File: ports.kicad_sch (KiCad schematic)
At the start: 0 parts

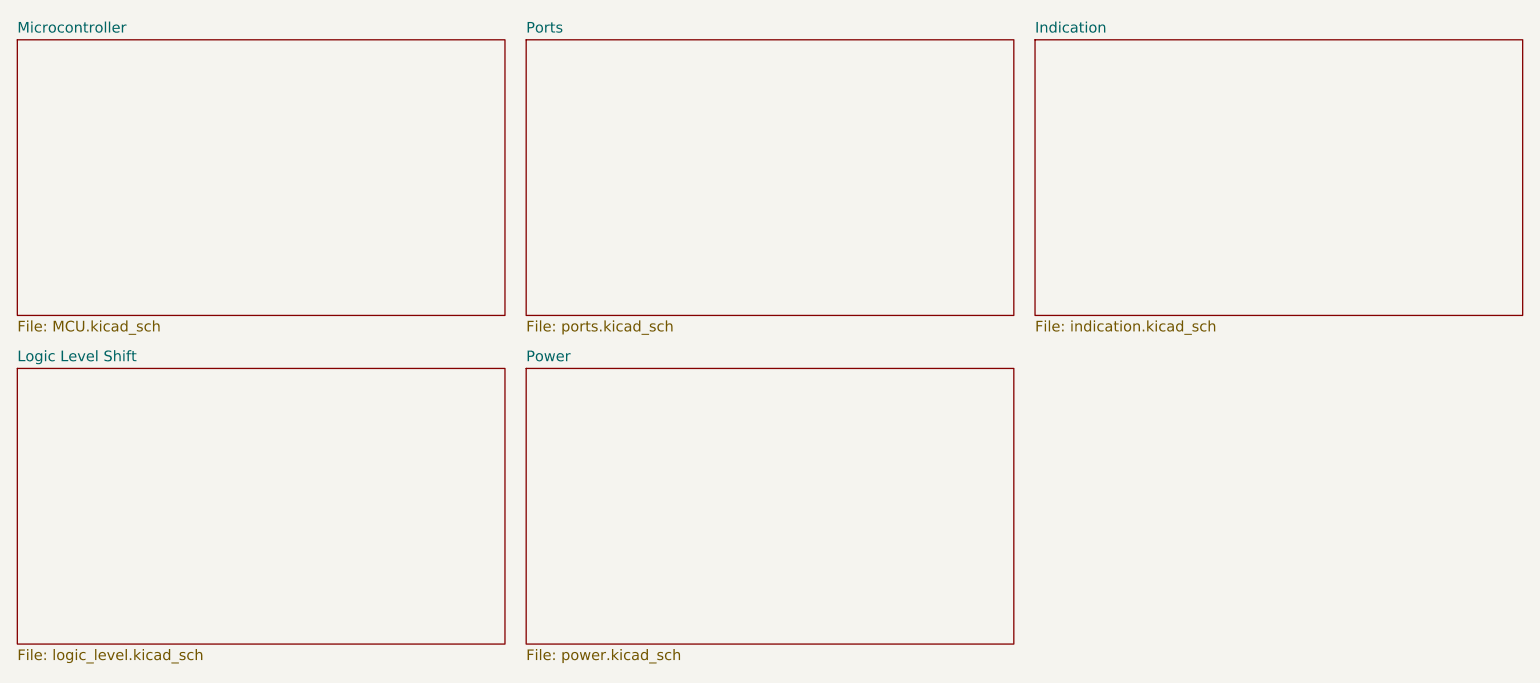
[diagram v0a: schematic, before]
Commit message: Break up schematic into hierarchical sheets
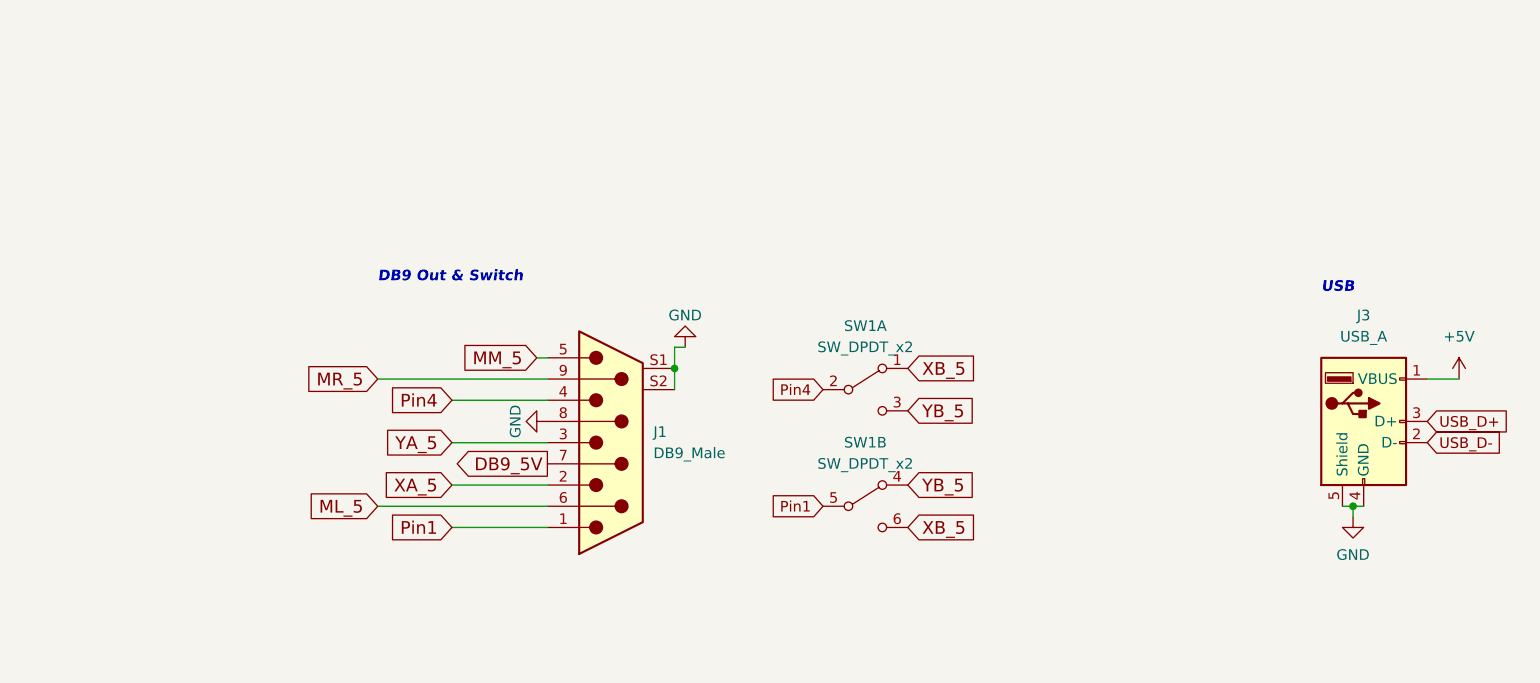
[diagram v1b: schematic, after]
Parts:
- added J1: DB9_Male, My Library:ASSMANN_A-DF_09_A_KG-T2S, symbol Connector:DB9_Male
- added J3: USB_A, Library:USB_A_China, symbol Connector:USB_A
- added SW1: SW_DPDT_x2, Button_Switch_SMD:SW_DPDT_CK_JS202011JCQN, symbol Switch:SW_DPDT_x2
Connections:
- new net +5V: J3.1 (VBUS)
- new net DB9_5V: J1.7
- new net GND: J1.8, J1.S1, J1.S2, J3.4 (GND), J3.5 (Shield)
- new net ML_5: J1.6
- new net MM_5: J1.5
- new net MR_5: J1.9
- new net Pin1: J1.1, SW1.5 (B)
- new net Pin4: J1.4, SW1.2 (B)
- new net USB_D+: J3.3 (D+)
- new net USB_D-: J3.2 (D-)
- new net XA_5: J1.2
- new net XB_5: SW1.1 (A), SW1.6 (C)
- new net YA_5: J1.3
- new net YB_5: SW1.3 (C), SW1.4 (A)
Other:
- removed sheet Indication
- removed sheet Logic Level Shift
- removed sheet Microcontroller
- removed sheet Ports
- removed sheet Power
- note added: "DB9 Out & Switch"
- note added: "USB"
